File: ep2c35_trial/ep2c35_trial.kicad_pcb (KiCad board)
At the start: 4 copper layers, 75.6 x 57.6 mm, 175 parts, among them J1 Conn_02x21_Odd_Even, J10 Conn_02x10_Odd_Even, J2 Conn_02x21_Odd_Even, J3 3M_8540-4500PL, J4 USB3_B_Micro_Amphenol_GSB343K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, J5 Conn_02x05_Odd_Even, J6 Conn_01x02_Male, J7 Conn_01x02_Male, J8 Conn_01x02_Male, J9 Conn_01x02_Male, U1 EP2C5F484, U10 SP3003-02UTG, U11 SP3003-02UTG, U12 SP3003-02UTG, U13 SP3003-02UTG, U14 SP3003-02UTG, U15 SP3003-02UTG, U16 SP3003-02UTG, U2 MIC37302, U3 FT600Q-B-T, U4 W25Q16JVSNIQ, U5 MIC39102, U6 MIC49150-1.2, U7 SP3003-02UTG, U8 SP3003-02UTG, U9 SP3003-02UTG, X1 FNETHE025, Y1 ABM7-30.000MHZ-D2Y-T

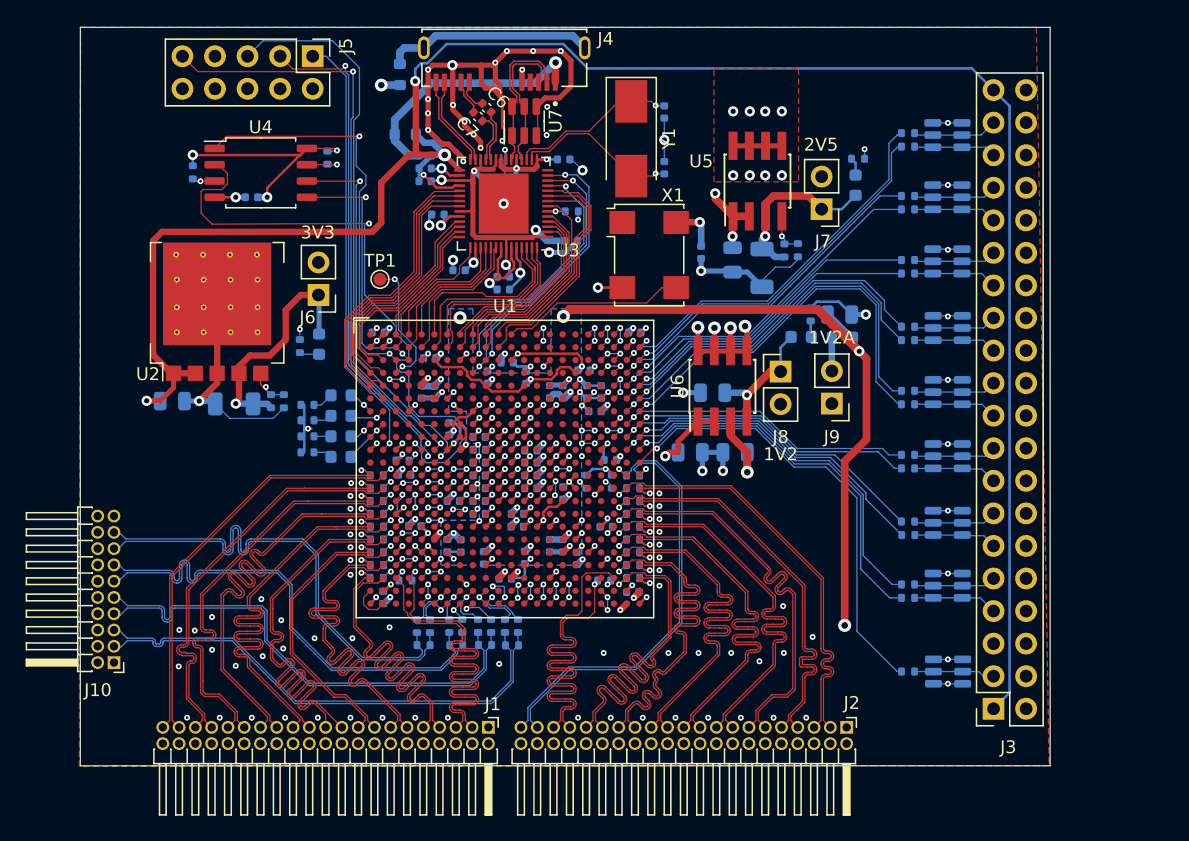
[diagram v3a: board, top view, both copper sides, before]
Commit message: Add LM317A power regulators.
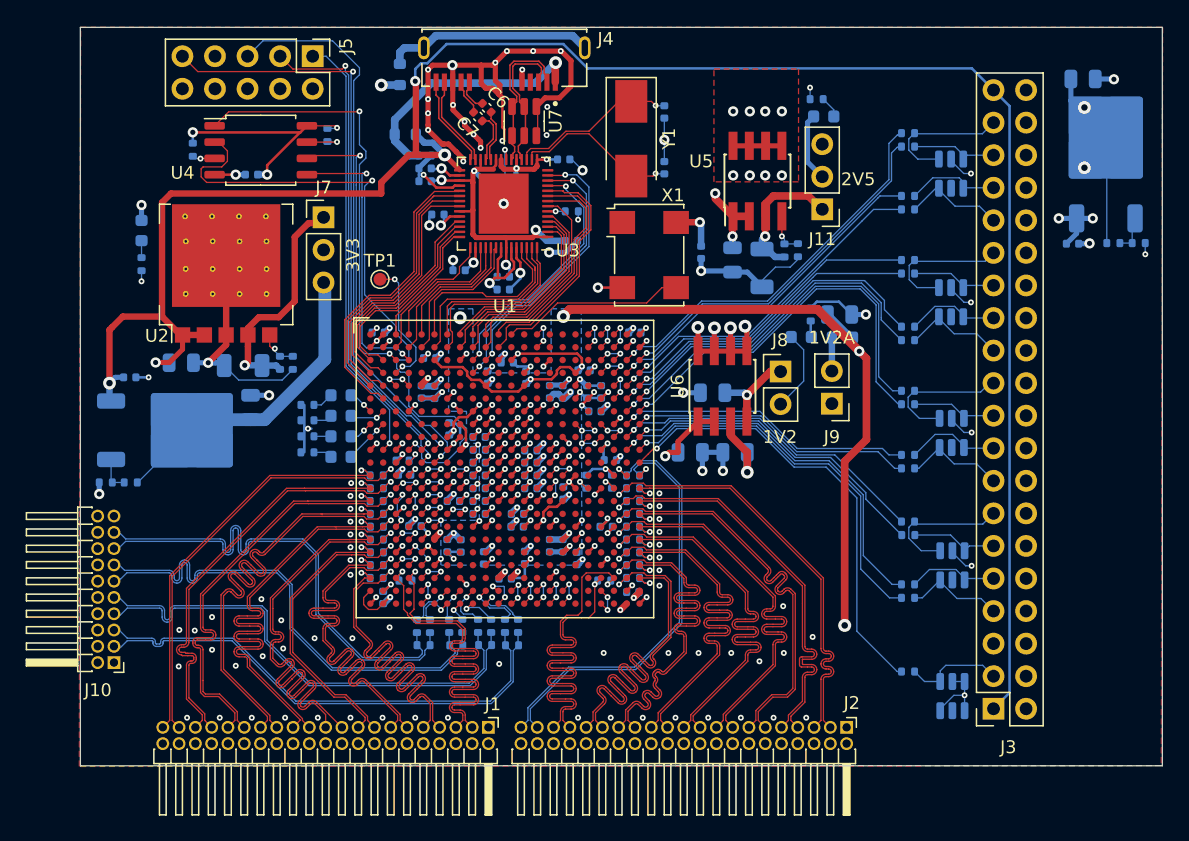
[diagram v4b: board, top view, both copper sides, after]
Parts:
- removed D2: LED, LED_SMD:LED_0603_1608Metric
- removed J6: Conn_01x02_Male, Connector_PinHeader_2.54mm:PinHeader_1x02_P2.54mm_Vertical
- removed R50: 1k, Resistor_SMD:R_0402_1005Metric
- removed U14, U15, U16: SP3003-02UTG, Package_TO_SOT_SMD:SOT-23-6
- added C21: 100n, Capacitor_SMD:C_0402_1005Metric, B.Cu at (188.8, 63.9)
- added C71: 1u, Capacitor_SMD:C_0805_2012Metric, B.Cu at (189.6, 51.1)
- added C72: 100n, Capacitor_SMD:C_0402_1005Metric, B.Cu at (115.2, 74.3)
- added C73: 1u, Capacitor_SMD:C_0805_2012Metric, B.Cu at (124.7, 76.7)
- added D8: LED, LED_SMD:LED_0603_1608Metric, B.Cu at (116.2, 62.9)
- added J11: Conn_01x03_Pin, Connector_PinHeader_2.54mm:PinHeader_1x03_P2.54mm_Vertical, F.Cu at (169.2, 61.2)
- added R68: 5k, Resistor_SMD:R_0402_1005Metric, B.Cu at (192.0, 63.9)
- added R69: 5k, Resistor_SMD:R_0402_1005Metric, B.Cu at (193.9, 63.9)
- added R70: 1k, Resistor_SMD:R_0402_1005Metric, B.Cu at (116.2, 65.5)
- added R71: 5k, Resistor_SMD:R_0402_1005Metric, B.Cu at (115.3, 82.5)
- added R72: 3k, Resistor_SMD:R_0402_1005Metric, B.Cu at (113.4, 82.5)
- added U17: SRV05-4, Package_TO_SOT_SMD:SOT-23-6, B.Cu at (179.3, 58.5)
- J7: value Conn_01x02_Male -> Conn_01x03_Pin; footprint Connector_PinHeader_2.54mm:PinHeader_1x02_P2.54mm_Vertical -> Connector_PinHeader_2.54mm:PinHeader_1x03_P2.54mm_Vertical
- U10, U11, U8, U9: value SP3003-02UTG -> SRV05-4
- U12, U13: value SP3003-02UTG -> LM317_TO-252; footprint Package_TO_SOT_SMD:SOT-23-6 -> Package_TO_SOT_SMD:TO-252-2
- moved U13 60.3 mm to (118.8, 78.5)
- moved R49 44.7 mm to (168.8, 52.6), turned to 0 degrees
- moved D1 43.2 mm to (169.4, 54.0), turned to 180 degrees
- moved J7 38.9 mm to (130.3, 61.9), turned to 0 degrees
- moved U11 28.7 mm to (179.4, 99.2), turned to -90 degrees
- moved U10 23.7 mm to (179.4, 89.0), turned to -90 degrees
- moved U12 22.3 mm to (191.4, 56.9), turned to 90 degrees
- moved U9 18.4 mm to (179.3, 78.7), turned to -90 degrees
- moved U8 13.0 mm to (179.3, 68.5), turned to -90 degrees
- moved C23 3.07 mm to (119.2, 73.2)
- moved C24 3.07 mm to (124.1, 73.4)
- moved R8 3.07 mm to (127.0, 73.2)
- moved R9 3.07 mm to (128.0, 73.2)
- moved U2 3.07 mm to (122.8, 67.7)
- moved C15 1.77 mm to (124.7, 58.5)
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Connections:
- D1 pad 2: /3V3_LDO -> +2V5
- D3 pad 2: /1V2_LDO -> +1V2
- J7 pad 1: /2V5_LDO -> /3V3_LDO
- J7 pad 2: +2V5 -> +3.3V
- U10 pad 1: /POD_D5 -> /POD_D12
- U10 pad 2: /POD_D4 -> GNDD
- U10 pad 3: GNDD -> /POD_D13
- U10 pad 4: GNDD -> /POD_D14
- U10 pad 5: /POD_D4 -> unconnected-(U10-VP-Pad5)
- U10 pad 6: /POD_D5 -> /POD_D15
- U11 pad 1: /POD_D7 -> /POD_CLK
- U11 pad 2: /POD_D6 -> GNDD
- U11 pad 5: /POD_D6 -> unconnected-(U11-VP-Pad5)
- U11 pad 6: /POD_D7 -> GNDD
- U12 pad 1: /POD_D9 -> /2V5_ADJ_LM
- U12 pad 2: /POD_D8 -> /2V5_LM_LDO
- U12 pad 3: GNDD -> +3.3V
- U13 pad 1: /POD_D11 -> /3V3_ADJ_LM
- U13 pad 2: /POD_D10 -> /3V3_LM_LDO
- U13 pad 3: GNDD -> /VBUS
- U8 pad 1: /POD_D1 -> /POD_D4
- U8 pad 2: /POD_D0 -> GNDD
- U8 pad 3: GNDD -> /POD_D5
- U8 pad 4: GNDD -> /POD_D6
- U8 pad 5: /POD_D0 -> unconnected-(U8-VP-Pad5)
- U8 pad 6: /POD_D1 -> /POD_D7
- U9 pad 1: /POD_D3 -> /POD_D8
- U9 pad 2: /POD_D2 -> GNDD
- U9 pad 3: GNDD -> /POD_D9
- U9 pad 4: GNDD -> /POD_D10
- U9 pad 5: /POD_D2 -> unconnected-(U9-VP-Pad5)
- U9 pad 6: /POD_D3 -> /POD_D11
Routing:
- net /3V3_LM_LDO: track 0.00 -> 20.1 mm
- net /2V5_LM_LDO: track 0.00 -> 11.7 mm, vias 0 -> 2
- net /VBUS: track 152.7 -> 160.8 mm, vias 3 -> 4
- net +1V2: track 33.8 -> 40.2 mm
- net +3.3V: track 102.7 -> 108.9 mm, vias 32 -> 35
- net +2V5: track 33.8 -> 39.2 mm
- net /POD_D12: track 6.51 -> 10.9 mm
- net /POD_D0: track 6.39 -> 10.7 mm
- net /POD_D8: track 6.49 -> 10.8 mm
- net /POD_D4: track 6.47 -> 10.8 mm
- net /2V5_LDO: track 14.5 -> 11.5 mm
- net /1V2_LDO: track 10.3 -> 7.25 mm
- net /2V5_ADJ_LM: track 0.00 -> 2.98 mm
- net /3V3_ADJ_LM: track 0.00 -> 2.76 mm
- net /SPI_DATA0: track 49.5 -> 51.9 mm
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- added copper zone on In2.Cu, net /2V5_LM_LDO
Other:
- board size 75.6 x 57.6 mm -> 84.4 x 57.6 mm
